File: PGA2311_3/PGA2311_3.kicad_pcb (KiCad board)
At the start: 2 copper layers, 234 x 58 mm, 205 parts, among them J201 3, J202 3, J203 2, J204 2, J301 Conn_01x16, J302 1, J303 Conn_01x02, J304 4, J305 4, J401 1, J402 3, J403 1, Q301 BC817-40, SW301 SW_Push, SW302 Encoder PEC11R, U201 OPA1678IDR, U202 CD74HCT4052, U203 CD74HCT4052, U204 LM337LM, U205 PGA2311UA, U206 LM317LIDR, U207 UA78L05AIDR, U301 TPS60403DBV, U302 WH1602B, U303 SN74LVC8T245DW, U304 STM32G070KBT6, U305 TLV1117-50IDC, U306 LP2985-33DBV, U307 SN74LVC2G17DBV

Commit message: Add files via upload
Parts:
- moved TP202 15.2 mm to (115.1, 22.9)
- moved J202 2.54 mm to (115.4, 28.4)
- moved TP201 0.45 mm to (115.0, 58.4)
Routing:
- net Net-(J202-Pin_2): track 9.50 -> 12.2 mm
- net Net-(J202-Pin_3): track 8.89 -> 6.94 mm
- net GND: vias 249 -> 247

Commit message: Add files via upload
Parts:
- moved C214 0.51 mm to (79.0, 49.1)
- moved R208 0.13 mm to (97.3, 52.3)
- moved R212 0.13 mm to (65.5, 36.6)
- moved C209 0.13 mm to (80.4, 25.5)
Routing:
- net Net-(U202-X0): track 42.9 -> 42.0 mm
- net GND: vias 247 -> 249

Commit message: Add files via upload
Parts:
- moved C214 0.63 mm to (79.0, 49.8)
- moved R233 0.13 mm to (47.5, 31.8)
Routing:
- net Net-(U201A--): track 25.3 -> 26.6 mm
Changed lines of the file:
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@@
 	(footprint "Resistor_SMD:R_0805_2012Metric_Pad1.20x1.40mm_HandSolder"
 		(layer "B.Cu")
-		(at 47.498 31.623 180)
+		(at 47.498 31.75 180)
 		(descr "Resistor SMD 0805 (2012 Metric), square (rectangular) end terminal, IPC-7351 nominal with elongated pad for handsoldering. (Body size source: IPC-SM-782 page 72, https://www.pcb-3d.com/wordpress/wp-content/uploads/ipc-sm-782a_amendment_1_and_2.pdf), generated with kicad-footprint-generator")
 		(tags "resistor handsolder")
@@
 	(footprint "Capacitor_SMD:C_0805_2012Metric_Pad1.18x1.45mm_HandSolder"
 		(layer "B.Cu")
-		(at 78.994 49.149 -90)
+		(at 78.994 49.784 -90)
 		(descr "Capacitor SMD 0805 (2012 Metric), square (rectangular) end terminal, IPC-7351 nominal with elongated pad for handsoldering. (Body size source: IPC-SM-782 page 76, https://www.pcb-3d.com/wordpress/wp-content/uploads/ipc-sm-782a_amendment_1_and_2.pdf, https://docs.google.com/spreadsheets/d/1BsfQQcO9C6DZCsRaXUlFlo91Tg2WpOkGARC1WS5S8t0/edit?usp=sharing), generated with kicad-footprint-generator")
 		(tags "capacitor handsolder")
@@
 	)
 	(via
-		(at 80.772 52.07)
+		(at 80.899 52.832)
 		(size 1)
 		(drill 0.5)
@@
 	(via
 		(at 46.95062 26.416)
-		(size 1)
-		(drill 0.5)
+		(size 1.5)
+		(drill 0.8)
 		(layers "F.Cu" "B.Cu")
 		(free yes)
@@
 	)
 	(via
-		(at 49.911 31.75)
+		(at 50.038 31.75)
 		(size 1)
 		(drill 0.5)
@@
 	(via
 		(at 67.818 63.627)
-		(size 1)
-		(drill 0.5)
+		(size 1.5)
+		(drill 0.8)
 		(layers "F.Cu" "B.Cu")
 		(free yes)
@@
 	)
 	(via
-		(at 80.518 29.718)
+		(at 81.026 29.21)
 		(size 1)
 		(drill 0.5)
@@
 	)
 	(via
-		(at 78.994 52.07)
+		(at 78.994 52.832)
 		(size 1)
 		(drill 0.5)
@@
 	)
 	(via
-		(at 78.867 31.623)
+		(at 78.867 32.512)
 		(size 1)
 		(drill 0.5)
@@
 		(start 73.533 46.736)
 		(end 72.12 46.736)
-		(width 0.5)
+		(width 0.75)
 		(layer "B.Cu")
 		(net 1)
@@
 	)
 	(segment
-		(start 69.7405 63.627)
-		(end 69.8675 63.627)
-		(width 0.5)
+		(start 50.038 31.75)
+		(end 48.498 31.75)
+		(width 0.75)
 		(layer "B.Cu")
 		(net 1)
 	)
 	(segment
-		(start 49.895 31.766)
-		(end 48.514 31.766)
+		(start 69.7405 63.627)
+		(end 69.8675 63.627)
 		(width 0.5)
 		(layer "B.Cu")
@@
 	)
 	(segment
-		(start 48.498 31.75)
-		(end 48.498 31.623)
-		(width 0.5)
-		(layer "B.Cu")
-		(net 1)
-	)
-	(segment
 		(start 37.338 39.116)
 		(end 37.338 37.7405)
@@
 	)
 	(segment
-		(start 48.514 31.766)
-		(end 48.498 31.75)
-		(width 0.5)
-		(layer "B.Cu")
-		(net 1)
-	)
-	(segment
 		(start 47.244 52.959)
 		(end 48.26 53.975)
@@
 	)
 	(segment
-		(start 49.911 31.75)
-		(end 49.895 31.766)
-		(width 0.5)
-		(layer "B.Cu")
-		(net 1)
-	)
-	(segment
 		(start 75.057 33.528)
 		(end 75.057 32.0255)
@@
 		(start 54.3052 46.863)
 		(end 55.642 46.863)
-		(width 0.5)
+		(width 0.75)
 		(layer "B.Cu")
 		(net 1)
@@
 	)
 	(segment
+		(start 44.45 31.75)
+		(end 46.498 31.75)
+		(width 0.75)
+		(layer "B.Cu")
+		(net 2)
+	)
+	(segment
 		(start 71.374 33.782)
 		(end 71.374 31.623)
@@
 	)
 	(segment
-		(start 46.498 31.623)
-		(end 46.498 29.591)
-		(width 0.75)
-		(layer "B.Cu")
-		(net 2)
-	)
-	(segment
 		(start 76.2 41.783)
 		(end 75.184 41.783)
@@
 	)
 	(segment
-		(start 44.45 31.75)
-		(end 46.371 31.75)
-		(width 0.75)
-		(layer "B.Cu")
-		(net 2)
-	)
-	(segment
-		(start 46.371 31.75)
-		(end 46.498 31.623)
-		(width 0.75)
-		(layer "B.Cu")
-		(net 2)
-	)
-	(segment
 		(start 40.1535 31.623)
 		(end 40.1535 35.306)
@@
 	)
 	(segment
+		(start 46.498 31.75)
+		(end 46.498 29.591)
+		(width 0.75)
+		(layer "B.Cu")
+		(net 2)
+	)
+	(segment
 		(start 41.656 44.577)
 		(end 40.1535 43.0745)
@@
 	)
 	(segment
+		(start 78.994 48.7465)
+		(end 78.994 47.625)
+		(width 0.75)
+		(layer "B.Cu")
+		(net 101)
+	)
+	(segment
+		(start 78.994 47.625)
+		(end 79.121 47.498)
+		(width 0.25)
+		(layer "B.Cu")
+		(net 101)
+	)
+	(segment
 		(start 77.089 47.498)
-		(end 84.901 47.498)
+		(end 79.121 47.498)
 		(width 0.5)
 		(layer "B.Cu")
@@
 		(width 0.5)
 		(layer "B.Cu")
+		(net 101)
+	)
+	(segment
+		(start 79.121 47.498)
+		(end 84.901 47.498)
+		(width 0.5)
+		(layer "B.Cu")

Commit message: Add files via upload
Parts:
- moved C310 0.25 mm to (169.7, 61.8)
- moved R314 0.13 mm to (172.2, 58.5)
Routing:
- net /analog/-5VA: track 132.8 -> 138.3 mm
- net /mcu/+3.3VD2: track 52.8 -> 51.9 mm
- net GND: vias 249 -> 250

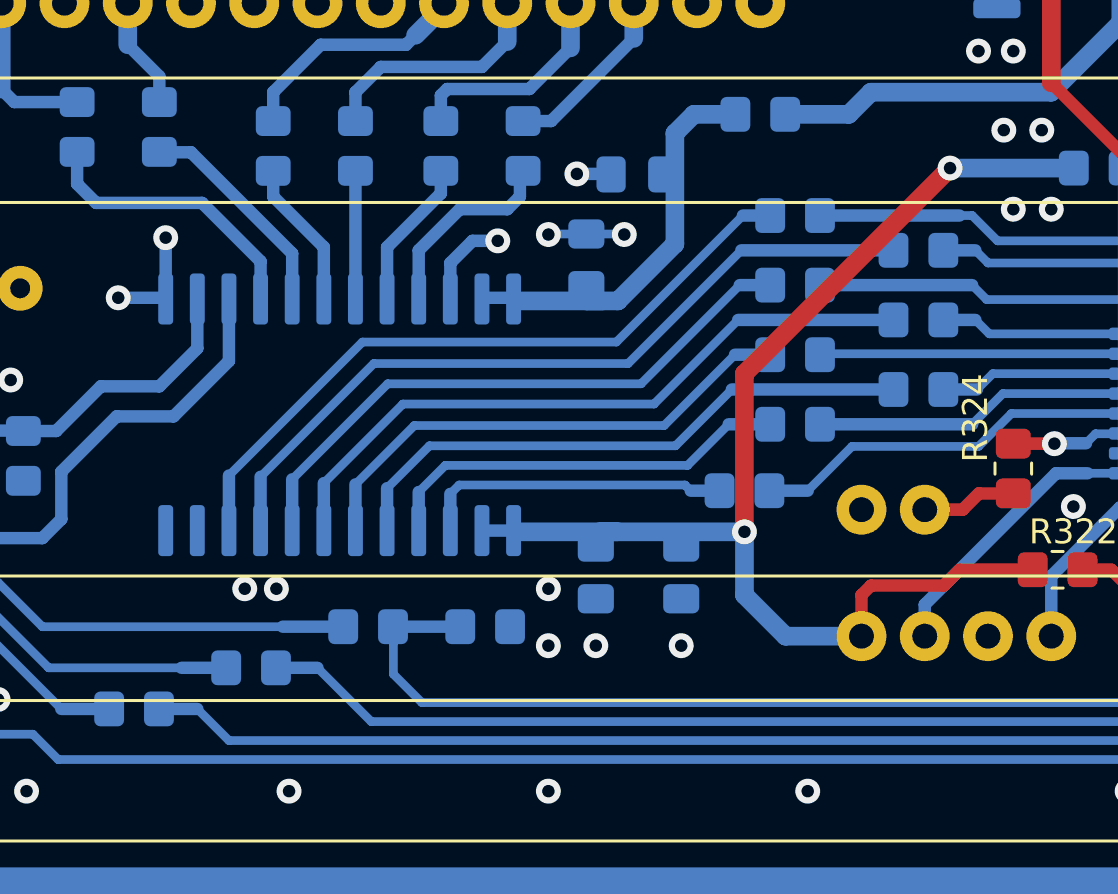
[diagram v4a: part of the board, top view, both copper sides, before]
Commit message: Add files via upload
added pull-up resistor for CS lines
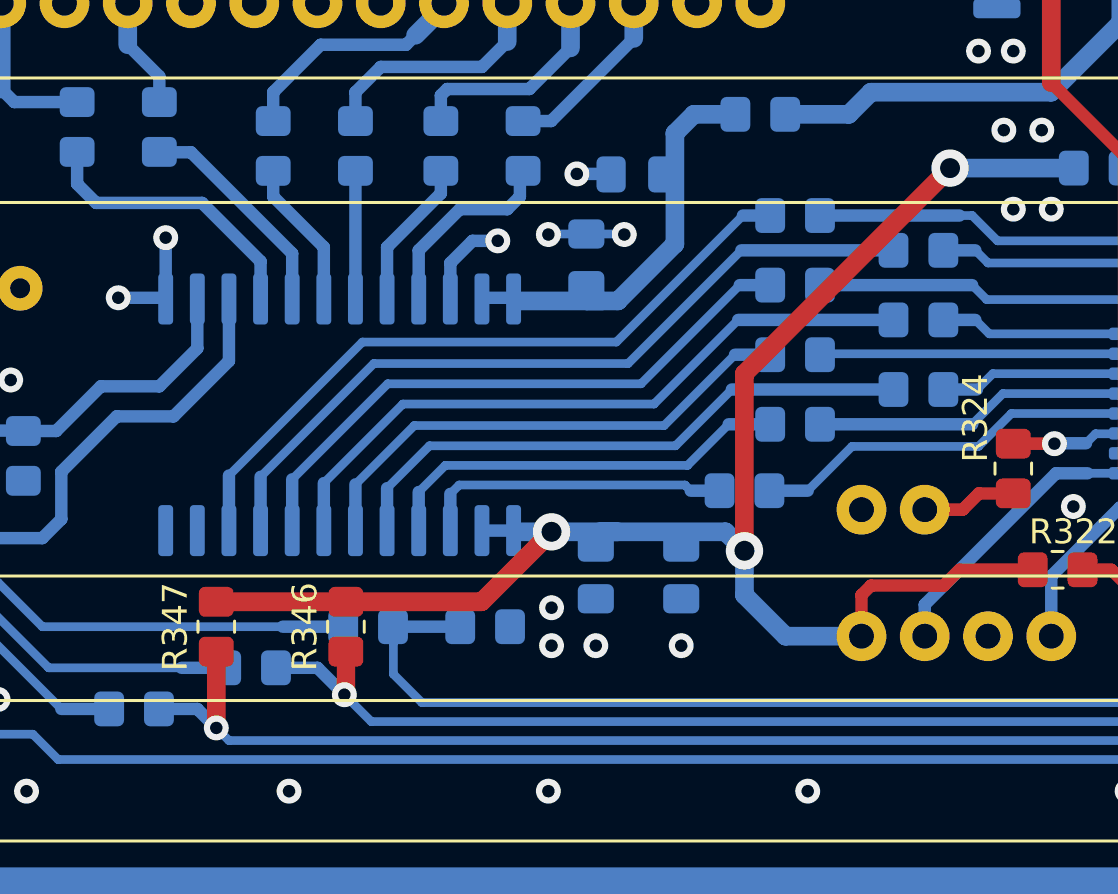
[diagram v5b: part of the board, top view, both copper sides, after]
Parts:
- added R346: 10k, Resistor_SMD:R_0805_2012Metric_Pad1.20x1.40mm_HandSolder, F.Cu at (156.2, 64.0)
- added R347: 10k, Resistor_SMD:R_0805_2012Metric_Pad1.20x1.40mm_HandSolder, F.Cu at (151.0, 64.0)
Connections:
- net Net-(U304-PA9/PA11) renamed /mcu/CS2
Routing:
- net /mcu/+3.3VD2: track 51.9 -> 66.8 mm, vias 2 -> 3
- net Net-(U304-PA8): track 54.6 -> 57.7 mm, vias 0 -> 1
- net /mcu/CS2: track 49.6 -> 51.5 mm, vias 0 -> 1
- net GND: vias 250 -> 248
